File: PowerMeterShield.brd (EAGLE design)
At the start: 59.7 x 53.3 mm, 16 parts, among them IC1 MCP3426A0-E/SN, IC2 INA138

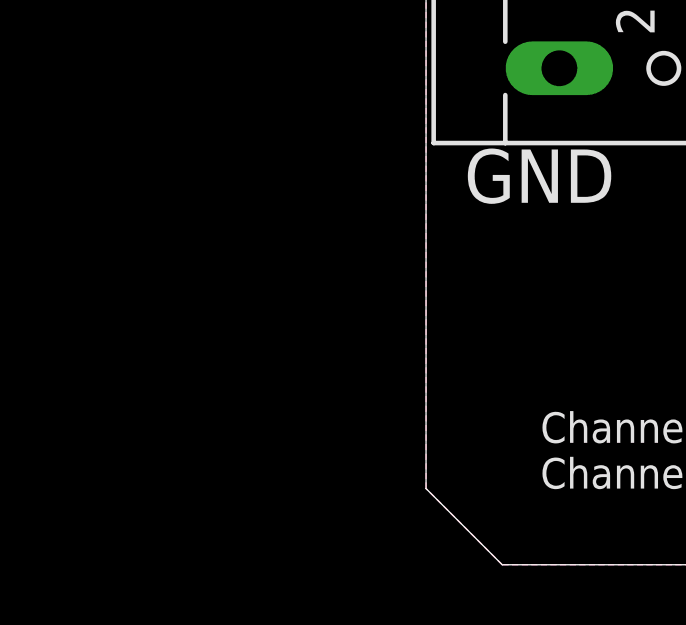
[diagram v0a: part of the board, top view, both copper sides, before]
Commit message: Added DC-DC converter to isolate circuit; still missing optocouplers and differential voltage measurement
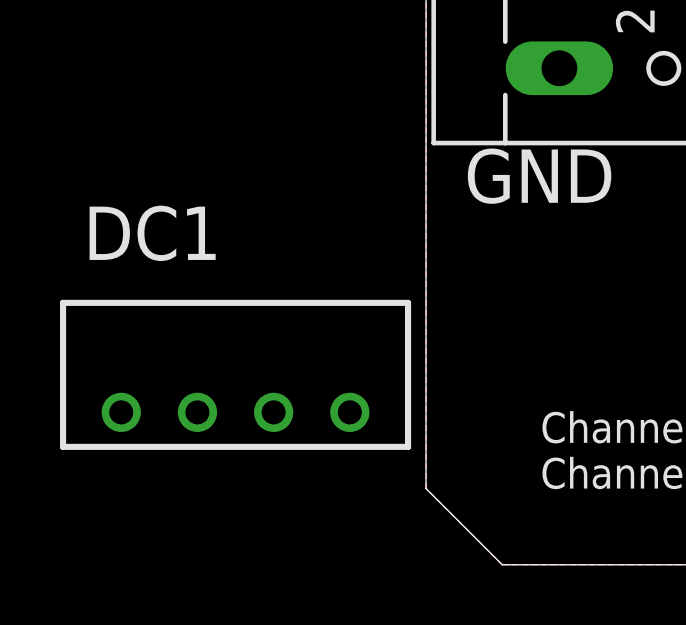
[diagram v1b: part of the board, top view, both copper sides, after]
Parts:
- added DC1: VA-0505S, dc-dc-converter:4SIL
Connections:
- new net +5V: DC1.2, JP3.4
- new net +5V/2: DC1.4
- new net GNDI: DC1.3
- net GND: now also DC1.1
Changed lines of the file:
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@@
 <attribute name="OC_FARNELL" value="2310707" x="37.465" y="31.4325" size="1.778" layer="27" display="off"/>
+</element>
+<element name="DC1" library="dc-dc-converter" package="4SIL" value="VA-0505S" x="-6.35" y="5.08">
+<attribute name="OC_NEWARK" value="unknown" x="-6.35" y="5.08" size="1.778" layer="27" display="off"/>
+<attribute name="MPN" value="" x="-6.35" y="5.08" size="1.778" layer="27" display="off"/>
+<attribute name="MF" value="" x="-6.35" y="5.08" size="1.778" layer="27" display="off"/>
+<attribute name="OC_FARNELL" value="unknown" x="-6.35" y="5.08" size="1.778" layer="27" display="off"/>
 </element>
 </elements>
@@
 <vertex x="57.15" y="0"/>
 </polygon>
+<contactref element="DC1" pad="1"/>
+<wire x1="21.59" y1="35.88" x2="17.78" y2="50.8" width="0" layer="19" extent="1-1"/>
+<wire x1="25.0825" y1="33.6525" x2="21.59" y2="35.88" width="0" layer="19" extent="1-1"/>
+<wire x1="24.13" y1="29.246" x2="25.0825" y2="33.6525" width="0" layer="19" extent="1-1"/>
+<wire x1="29.3878" y1="29.21" x2="24.13" y2="29.246" width="0" layer="19" extent="1-1"/>
+<wire x1="29.3878" y1="26.67" x2="29.3878" y2="29.21" width="0" layer="19" extent="1-1"/>
+<wire x1="34.1122" y1="27.94" x2="29.3878" y2="29.21" width="0" layer="19" extent="1-1"/>
+<wire x1="38.415" y1="31.4325" x2="34.1122" y2="27.94" width="0" layer="19" extent="1-1"/>
+<wire x1="4.445" y1="31.79" x2="21.59" y2="35.88" width="0" layer="19" extent="1-1"/>
+<wire x1="4.445" y1="16.55" x2="4.445" y2="31.79" width="0" layer="19" extent="1-1"/>
+<wire x1="-10.16" y1="5.08" x2="4.445" y2="16.55" width="0" layer="19" extent="1-1"/>
+<wire x1="31.75" y1="2.54" x2="29.3878" y2="26.67" width="0" layer="19" extent="1-1"/>
+<wire x1="34.29" y1="2.54" x2="31.75" y2="2.54" width="0" layer="19" extent="1-1"/>
 </signal>
 <signal name="ADC1">
@@
 <wire x1="30.479996875" y1="36.83" x2="28.61175" y2="38.698246875" width="0.254" layer="1"/>
 </signal>
+<signal name="+5V">
+<contactref element="JP3" pad="4"/>
+<contactref element="DC1" pad="2"/>
+<wire x1="-7.62" y1="5.08" x2="29.21" y2="2.54" width="0" layer="19" extent="1-1"/>
+</signal>
+<signal name="GNDI">
+<contactref element="DC1" pad="3"/>
+</signal>
+<signal name="+5V/2">
+<contactref element="DC1" pad="4"/>
+</signal>
 </signals>

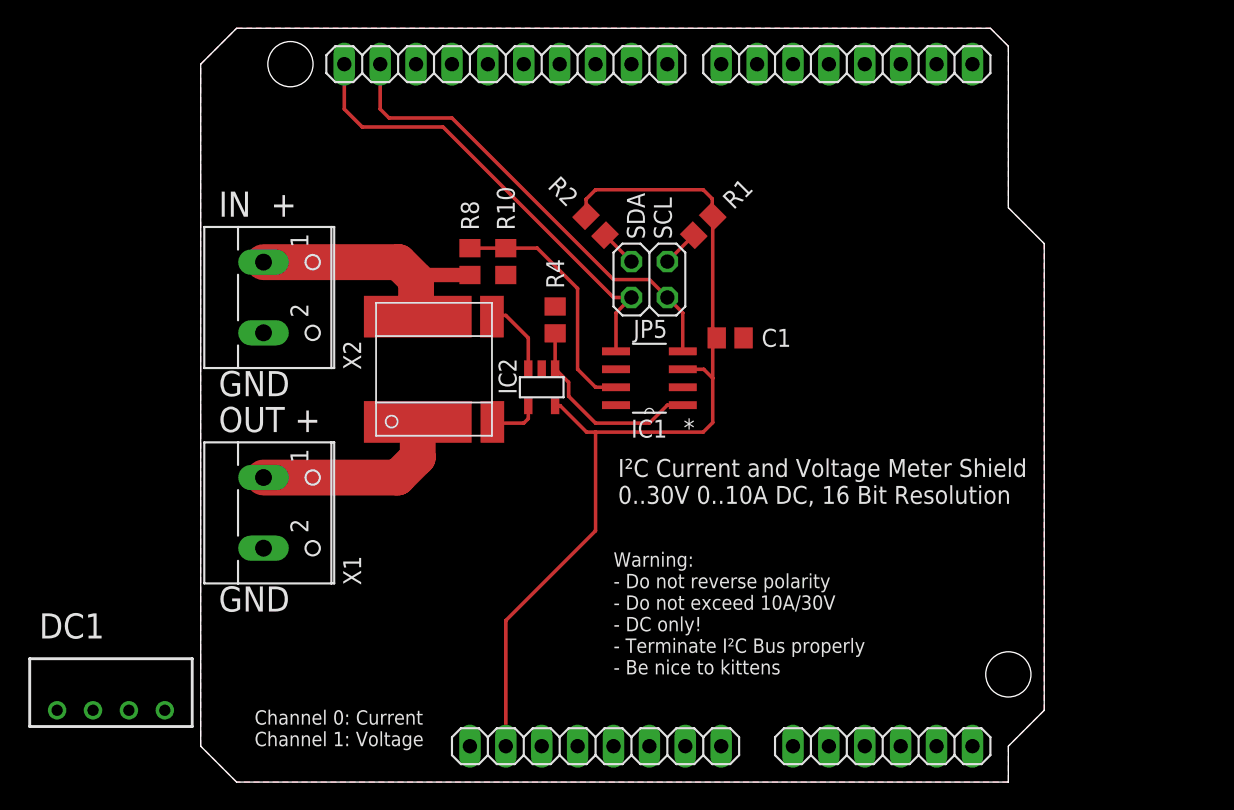
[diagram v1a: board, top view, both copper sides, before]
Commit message: Added I²C isolation
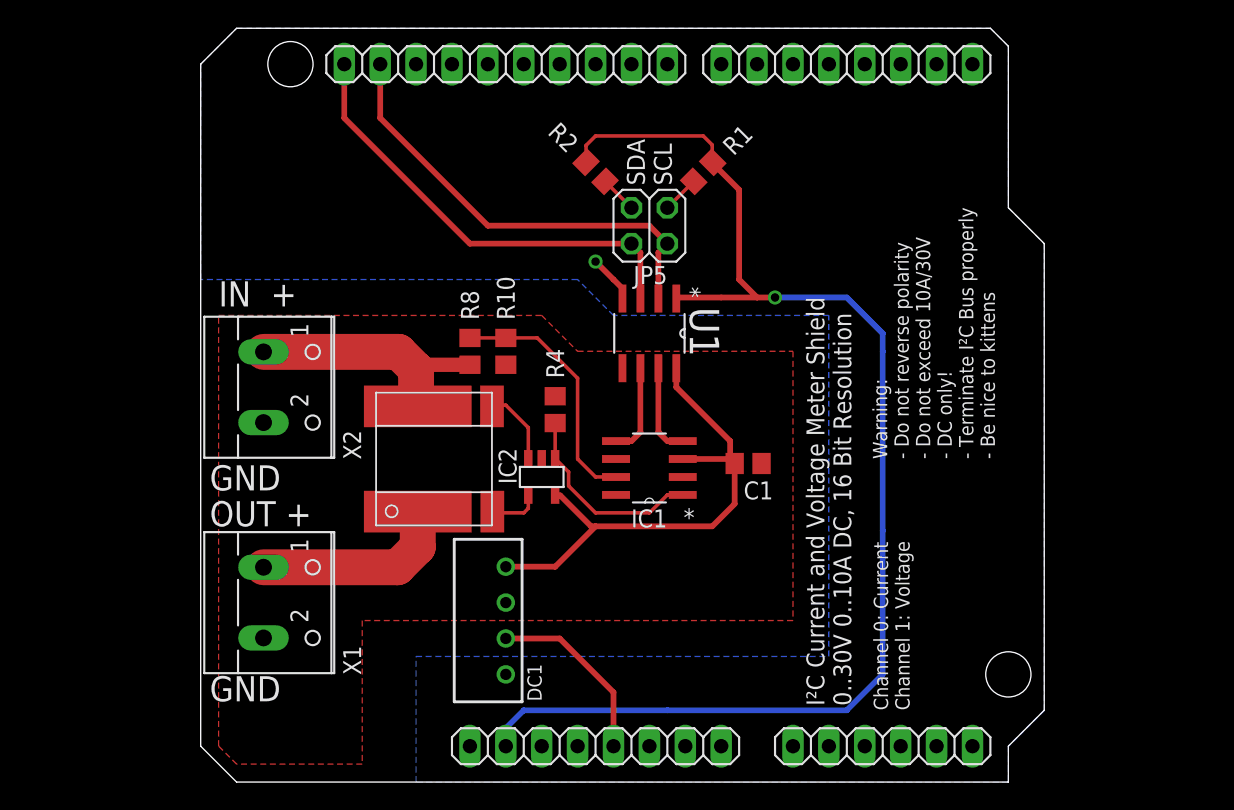
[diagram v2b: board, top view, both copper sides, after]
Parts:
- added U1: ADUM1250ARZ, Adum1250:SOIC127P600X175-8N
- moved DC1 28.7 mm to (21.6, 11.4), turned to 90 degrees
- moved C1 8.98 mm to (38.7, 22.5)
- moved IC2 6.35 mm to (24.1, 21.6)
- moved R4 6.35 mm to (25.1, 26.4)
- moved RS1 6.35 mm to (16.5, 22.9)
- moved X1 6.35 mm to (5.71, 12.7)
- moved IC1 6.35 mm to (31.8, 22.2)
- moved R10 6.35 mm to (21.6, 30.5)
- moved R8 6.35 mm to (19.1, 30.5)
- moved X2 6.35 mm to (5.71, 27.9)
- moved R1 3.81 mm to (35.6, 43.2)
- moved R2 3.81 mm to (27.9, 43.2)
- moved JP5 3.81 mm to (31.8, 39.4)
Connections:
- new net SCLI: IC1.5, U1.6
- new net SDAI: IC1.4, U1.7
- net +5V/2: now also C1.1, IC1.3, IC2.5, U1.8
- net GND: now also U1.4; no longer C1.2, IC1.2, IC1.6, IC1.8, IC2.2, R10.1, R4.1, X1.2, X2.2
- net GNDI: now also C1.2, IC1.2, IC1.6, IC1.8, IC2.2, R10.1, R4.1, U1.5, X1.2, X2.2
- net IOREF: now also U1.1; no longer C1.1, IC1.3, IC2.5
- net SCL: now also U1.3; no longer IC1.5
- net SDA: now also U1.2; no longer IC1.4
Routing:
- net +5V/2: track 0.00 -> 36.9 mm
- net IOREF: track 66.2 -> 92.1 mm, vias 0 -> 1
- net +5V: track 0.00 -> 13.0 mm
- net SDAI: track 0.00 -> 6.51 mm
- net SCLI: track 0.00 -> 6.51 mm
- net GND: track 0.00 -> 3.41 mm, vias 0 -> 1
- net SCL: track 33.3 -> 32.0 mm
- net SDA: track 33.3 -> 32.0 mm
- added copper zone on layer 1, net GNDI
- removed copper zone on layer 1, net GND

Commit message: Added creepage distance of about 3mm for a bit of safety™
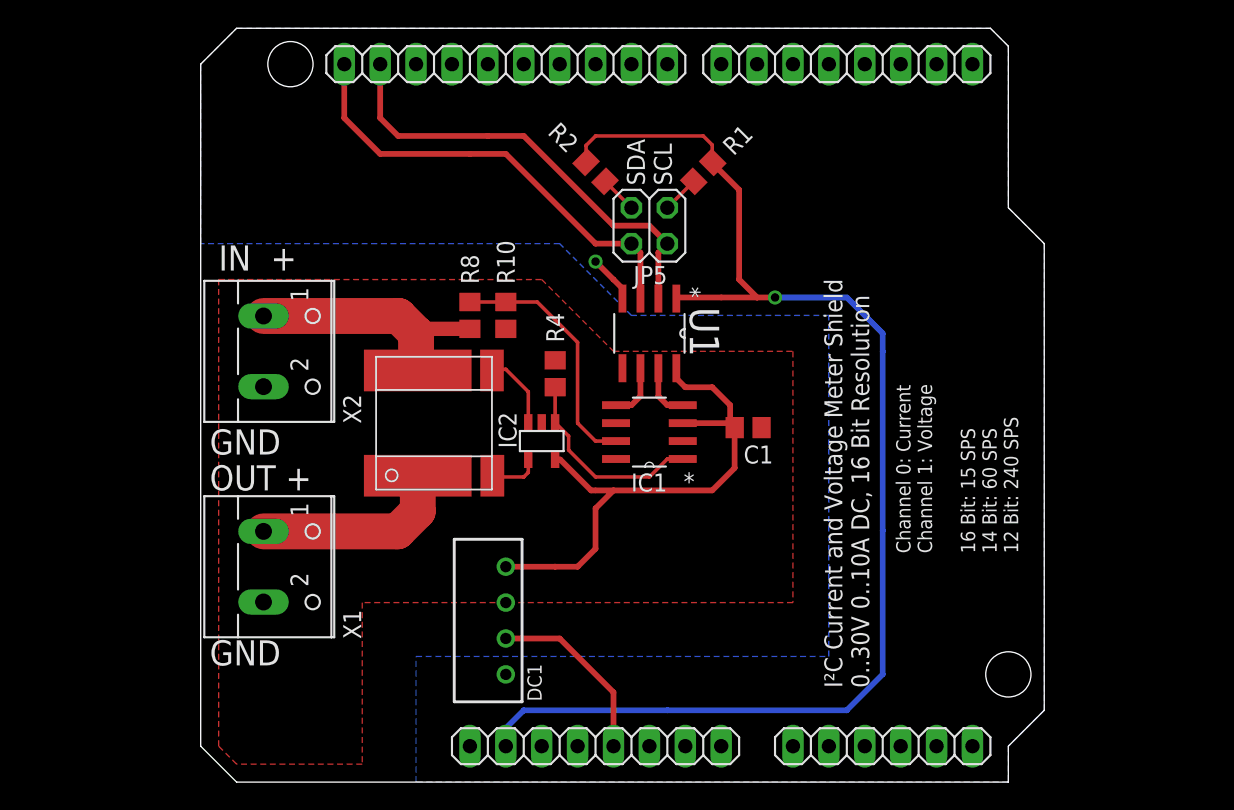
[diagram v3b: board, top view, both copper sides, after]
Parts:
- moved R10 2.54 mm to (21.6, 33.0)
- moved R8 2.54 mm to (19.1, 33.0)
- moved X1 2.54 mm to (5.71, 15.2)
- moved C1 2.54 mm to (38.7, 25.1)
- moved IC1 2.54 mm to (31.8, 24.8)
- moved IC2 2.54 mm to (24.1, 24.1)
- moved R4 2.54 mm to (25.1, 28.9)
- moved RS1 2.54 mm to (16.5, 25.4)
- moved X2 2.54 mm to (5.71, 30.5)
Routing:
- net +5V/2: track 36.9 -> 39.5 mm
- net SDAI: track 6.51 -> 3.97 mm
- net SCLI: track 6.51 -> 3.97 mm
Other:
- board text added: "Channel 0: Current Channel 1: Voltage 16 Bit: 15 SPS 14 Bit: 60 SPS 12 Bit: 240 SPS"
- board text removed: "Channel 0: Current Channel 1: Voltage"
- board text removed: "Warning: - Do not reverse polarity - Do not exceed 10A/30V - DC only! - Terminate I²C Bus properly - Be nice to kittens"

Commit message: Finalized design, made PCB larger in order to compensate for heigher components than the headers, so users can stack other shields on top of ours (hopefully).
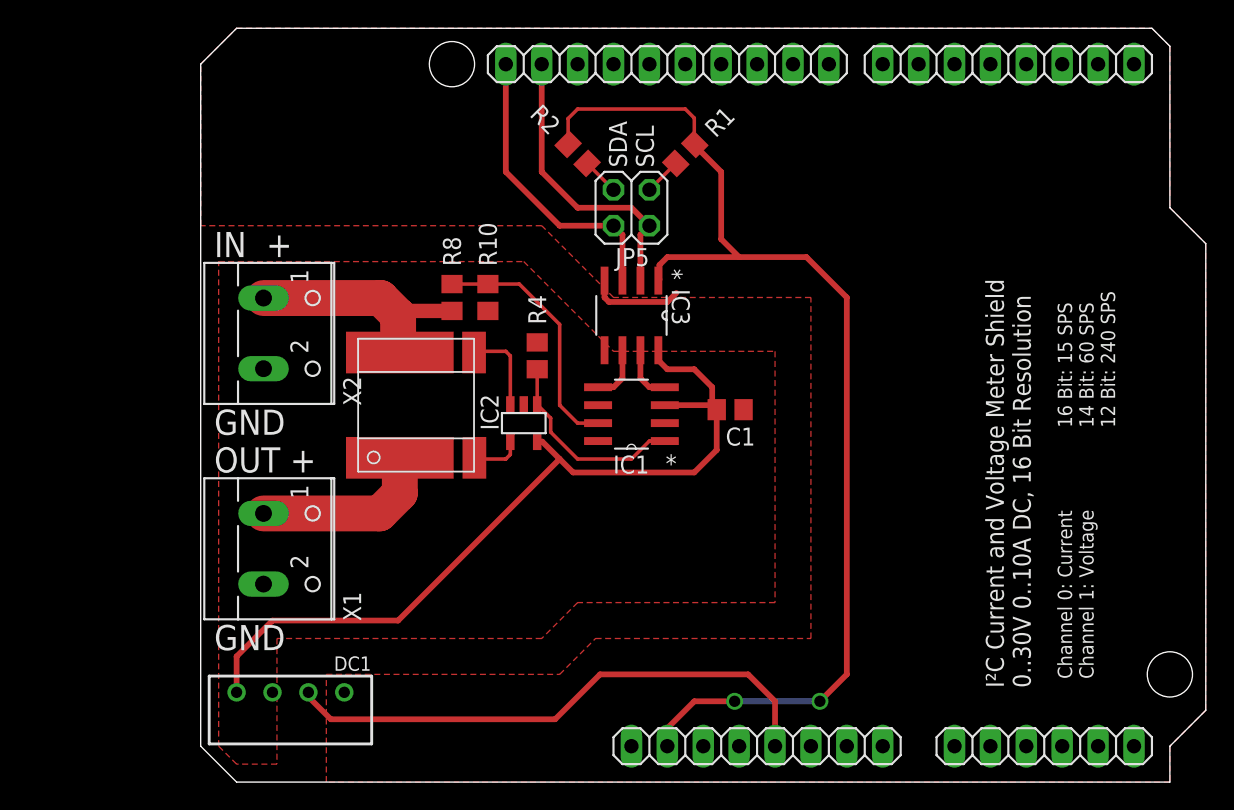
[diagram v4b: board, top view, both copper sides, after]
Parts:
- removed U1: ADUM1250ARZ, Adum1250:SOIC127P600X175-8N
- added IC3: ADUM1250ARZ, Adum1250:SOIC127P600X175-8N
- moved DC1 16.1 mm to (6.35, 6.35), turned to 180 degrees
- moved JP1 11.4 mm to (33.0, 50.8)
- moved JP2 11.4 mm to (57.1, 50.8)
- moved JP4 11.4 mm to (59.7, 2.54)
- moved JP3 11.4 mm to (39.4, 2.54)
- moved R1 1.80 mm to (34.3, 44.5)
- moved RS1 1.80 mm to (15.2, 26.7)
- moved JP5 1.80 mm to (30.5, 40.6)
- moved R2 1.80 mm to (26.7, 44.5)
- moved R4 1.80 mm to (23.8, 30.2)
- moved IC1 1.80 mm to (30.5, 26.0)
- moved IC2 1.80 mm to (22.9, 25.4)
- moved C1 1.80 mm to (37.5, 26.4)
- moved R10 1.80 mm to (20.3, 34.3)
- moved R8 1.80 mm to (17.8, 34.3)
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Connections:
- net +5V/2: now also IC3.8; no longer U1.8
- net GND: now also IC3.4; no longer U1.4
- net GNDI: now also IC3.5; no longer U1.5
- net IOREF: now also IC3.1; no longer U1.1
- net SCL: now also IC3.3; no longer U1.3
- net SCLI: now also IC3.6; no longer U1.6
- net SDA: now also IC3.2; no longer U1.2
- net SDAI: now also IC3.7; no longer U1.7
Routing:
- net +5V: track 13.0 -> 39.3 mm
- net +5V/2: track 39.5 -> 59.1 mm
- net IOREF: track 92.1 -> 80.5 mm, vias 1 -> 2
- net SDA: track 32.0 -> 21.0 mm
- net SCL: track 32.0 -> 21.0 mm
- net GND: track 3.41 -> 7.38 mm, vias 1 -> 0
- net N$5: track 14.0 -> 12.7 mm
- net VIN_MEAS: track 17.9 -> 16.7 mm
- net N$1: track 5.45 -> 6.19 mm
- added copper zone on layer 1, net GND
- removed copper zone on layer 16, net GND
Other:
- board size 59.7 x 53.3 mm -> 71.1 x 53.3 mm
- board text added: "16 Bit: 15 SPS 14 Bit: 60 SPS 12 Bit: 240 SPS"
- board text added: "Channel 0: Current Channel 1: Voltage"
- board text removed: "Channel 0: Current Channel 1: Voltage 16 Bit: 15 SPS 14 Bit: 60 SPS 12 Bit: 240 SPS"

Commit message: Updated to a modified design for differential voltage measurement
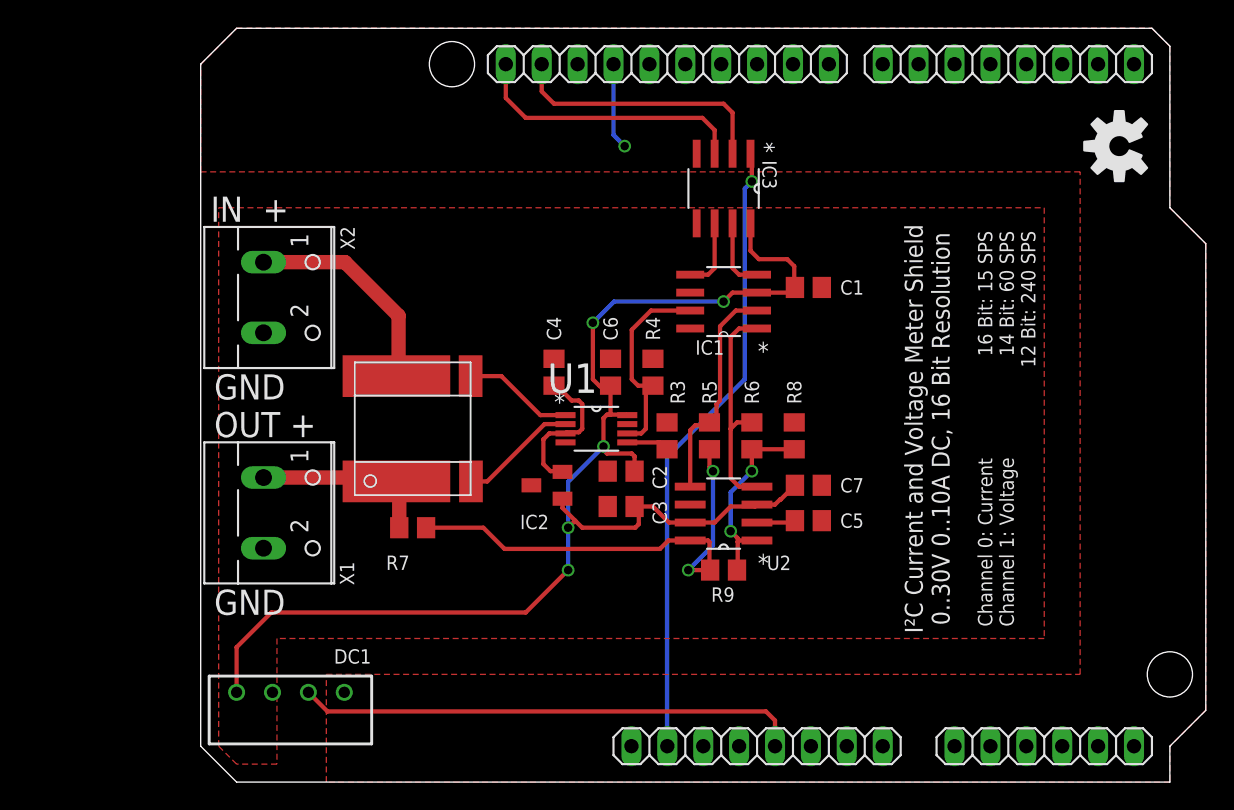
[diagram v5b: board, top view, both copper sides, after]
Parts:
- removed JP5: (no value), pinhead:2X02
- removed R1, R2: 4.7k, rcl:R0805
- removed R10: 68k, rcl:R0805
- added C2, C4, C5: 10n, rcl:C0805
- added C3: 10µ, rcl:C0805
- added C6, C7: 100n, rcl:C0805
- added R3: 20k, rcl:R0805
- added R5, R6: 200k, rcl:R0805
- added R7: 6.04M, rcl:R0805
- added R9: 412k, rcl:R0805
- added U$1: (no value), SparkFun:OSHW-LOGO-M
- added U1: INA170EA/2K5, INA170:SOP65P490X110-8N
- added U2: THS4521, THS4531:SOIC127P600X175-8N
- IC2: value INA138 -> ISL21080; device burr-brown:SOT23-5 -> maxim:SOT23
- R4: value 200k -> 20k
- R8: value 1M -> 6.04M
- moved R8 26.1 mm to (42.0, 24.5)
- moved IC3 11.1 mm to (37.0, 42.0)
- moved IC1 10.3 mm to (37.0, 34.0)
- moved C1 10.3 mm to (43.0, 35.0)
- moved R4 8.27 mm to (32.0, 29.0)
- moved IC2 4.70 mm to (24.5, 21.0), turned to 90 degrees
- moved X1 2.54 mm to (5.71, 19.1)
- moved X2 2.54 mm to (5.71, 34.3)
- moved RS1 1.69 mm to (15.0, 25.0)
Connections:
- removed net ADC1: IC1.1, IC2.1, R4.2
- removed net N$3: JP5.1, R1.2
- removed net N$4: JP5.3, R2.2
- removed net N$5: RS1.I2, X1.1
- new net ADC1+: IC1.1, R6.2, U2.4
- new net ADC1-: IC1.2, R5.2, U2.5
- new net CURRENT+: RS1.S2, U1.2
- new net CURRENT-: RS1.S1, U1.1
- new net N$10: R6.1, R8.2, R9.1, U2.1
- new net N$7: R3.2, U1.5
- new net REF: C4.2, IC2.2, U1.3
- new net V_MEAS: R7.1, RS1.I2, X1.1
- net +5V/2: now also C2.1, C3.1, C6.1, C7.1, IC2.1, U1.8, U2.3, U2.7; no longer IC2.5
- net ADC2: now also R4.2, U1.6; no longer R10.2, R8.1
- net GNDI: now also C2.2, C3.2, C4.1, C5.1, C6.2, C7.2, IC2.3, R3.1, R8.1, U1.4, U2.6; no longer IC1.2, IC2.2, R10.1
- net IOREF: no longer R1.1, R2.1
- net N$1: now also C5.2, U2.2; no longer IC2.3, RS1.S1
- net N$2: now also R5.1, R7.2, R9.2, U2.8; no longer IC2.4, RS1.S2
- net SCL: no longer JP5.4
- net SDA: no longer JP5.2
- net VIN_MEAS: no longer R8.2
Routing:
- net +5V/2: track 59.1 -> 97.9 mm, vias 0 -> 5
- net IOREF: track 80.5 -> 44.5 mm, vias 2 -> 1
- net N$2: track 3.63 -> 33.9 mm, vias 0 -> 2
- net ADC1+: track 0.00 -> 15.9 mm
- net ADC1-: track 0.00 -> 15.8 mm
- net ADC1: track 14.2 -> 0.00 mm
- net N$10: track 0.00 -> 13.9 mm, vias 0 -> 2
- net V_MEAS: track 0.00 -> 12.9 mm
- net N$5: track 12.7 -> 0.00 mm
- net REF: track 0.00 -> 10.7 mm
- net CURRENT+: track 0.00 -> 8.37 mm
- net CURRENT-: track 0.00 -> 7.86 mm
- net +5V: track 39.3 -> 35.7 mm
- net N$1: track 6.19 -> 2.74 mm
- net ADC2: track 17.8 -> 14.6 mm
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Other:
- board text removed: "SDA SCL"

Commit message: Added domain name + descriptions for the functional schematic blocks
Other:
- board text added: "www.felitek.de"
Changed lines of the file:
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@@
 14 Bit: 60 SPS
 12 Bit: 240 SPS</text>
+<text x="63" y="11" size="1.016" layer="25" rot="R90" align="top-left">www.felitek.de
+</text>
 </plain>
 <attributes>
